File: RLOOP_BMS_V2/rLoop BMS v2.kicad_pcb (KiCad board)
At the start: 2 copper layers, 77.5 x 133 mm, 274 parts, among them IC1 FXO-HC736R-1.000, IC2 SN74AUP1G74DCUR, IC3 ATA6870N-PLQW-1, IC4 ATA6870N-PLQW-1, IC5 ATA6870N-PLQW-1, J1 CONN_02X07, J2 2-640387-0, Q1 FDN337N, Q10 PMV20ENR, Q11 PMV20ENR, Q12 PMV20ENR, Q13 PMV20ENR, Q14 PMV20ENR, Q15 PMV20ENR, Q16 PMV20ENR, Q17 PMV20ENR, Q18 PMV20ENR, Q19 PMV20ENR, Q2 PMV20ENR, Q3 PMV20ENR, Q4 PMV20ENR, Q5 PMV20ENR, Q6 PMV20ENR, Q7 PMV20ENR, Q8 PMV20ENR, Q9 PMV20ENR, U1 VOS618A-2X001T

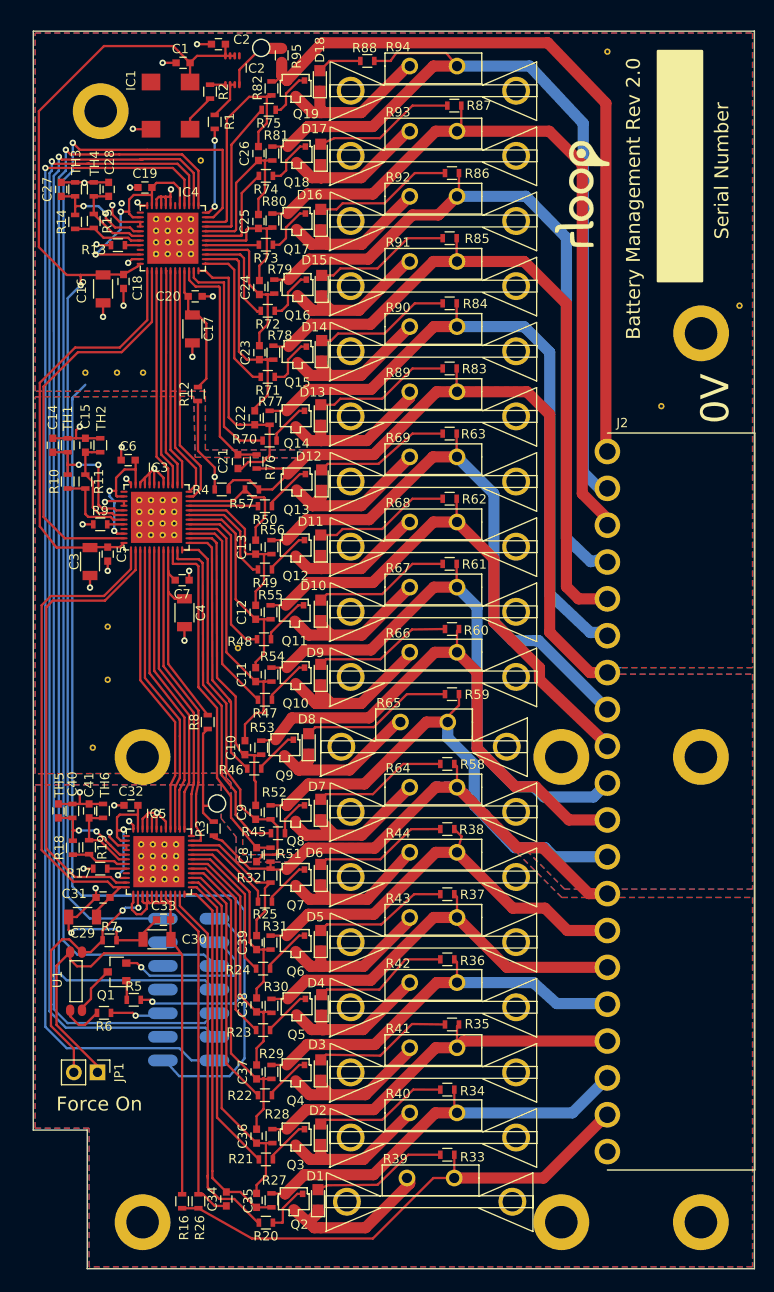
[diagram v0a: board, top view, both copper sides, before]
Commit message: Ti BMS WIP
Getting there. Need to add temp sensors, fan control, and an LDO for the
SPI ISO supply.
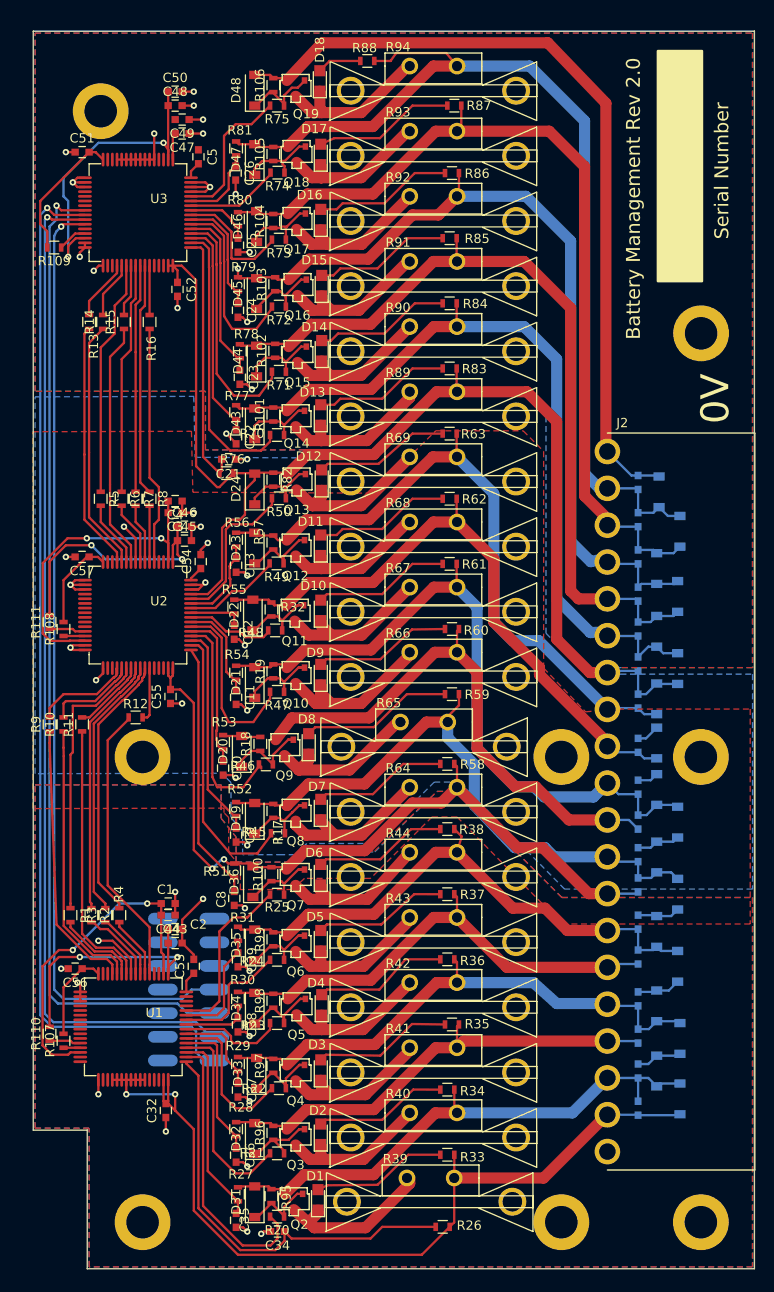
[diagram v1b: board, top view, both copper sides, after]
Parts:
- removed G***: LOGO, rLoop_Footprints:rLoop_Logo
- removed IC1: FXO-HC736R-1.000, rLoop_Footprints:Oscillator_SMD_FOX_HC3_4pin_7.0x5.0mm
- removed IC2: SN74AUP1G74DCUR, rLoop_Footprints:TI_sn74aup1g74_UQFN-0.6mm
- removed IC3, IC4, IC5: ATA6870N-PLQW-1, rLoop_Footprints:ATA6870-QFN48
- removed JP1: Debug Jumper, Pin_Headers:Pin_Header_Straight_1x02_Pitch2.54mm
- removed Q1: FDN337N, TO_SOT_Packages_SMD:SOT-23
- removed the REF** at (67.0, 64.5)
- removed the REF** at (65.7, 64.5)
- removed the REF** at (64.5, 64.5)
- removed the REF** at (63.2, 64.5)
- removed the REF** at (67.0, 63.2)
- removed the REF** at (65.7, 63.2)
- removed the REF** at (64.5, 63.2)
- removed the REF** at (63.2, 63.2)
- removed the REF** at (65.2, 97.2)
- removed the REF** at (63.9, 97.2)
- removed the REF** at (67.0, 67.0)
- removed the REF** at (62.6, 97.2)
- removed the REF** at (61.4, 97.2)
- removed the REF** at (65.2, 95.9)
- removed the REF** at (63.9, 95.9)
- removed the REF** at (62.6, 95.9)
- removed the REF** at (61.4, 95.9)
- removed the REF** at (65.2, 94.7)
- removed the REF** at (63.9, 94.7)
- removed the REF** at (62.6, 94.7)
- removed the REF** at (61.4, 94.7)
- removed the REF** at (65.7, 67.0)
- removed the REF** at (65.2, 93.4)
- removed the REF** at (63.9, 93.4)
- removed the REF** at (62.6, 93.4)
- removed the REF** at (61.4, 93.4)
- removed the REF** at (65.3, 134.2)
- removed the REF** at (64.1, 134.2)
- removed the REF** at (62.9, 134.2)
- removed the REF** at (61.6, 134.2)
- removed the REF** at (65.3, 132.9)
- removed the REF** at (64.1, 132.9)
- removed the REF** at (64.5, 67.0)
- removed the REF** at (62.9, 132.9)
- removed the REF** at (61.6, 132.9)
- removed the REF** at (65.3, 131.7)
- removed the REF** at (64.1, 131.7)
- removed the REF** at (62.9, 131.7)
- removed the REF** at (61.6, 131.7)
- removed the REF** at (65.3, 130.4)
- removed the REF** at (64.1, 130.4)
- removed the REF** at (62.9, 130.4)
- removed the REF** at (61.6, 130.4)
- removed the REF** at (63.2, 67.0)
- removed the REF** at (117.5, 83.3)
- removed the REF** at (125.9, 72.5)
- removed the REF** at (111.7, 45.2)
- removed the REF** at (72.0, 109.3)
- removed the REF** at (56.4, 120.0)
- removed the REF** at (58.0, 112.7)
- removed the REF** at (58.0, 107.0)
- removed the REF** at (61.8, 79.7)
- removed the REF** at (59.0, 79.7)
- removed the REF** at (55.6, 79.7)
- removed the REF** at (67.0, 65.7)
- removed the REF** at (68.0, 56.9)
- removed the REF** at (65.7, 65.7)
- removed the REF** at (64.5, 65.7)
- removed the REF** at (63.2, 65.7)
- removed TH1, TH2, TH3, TH4, TH5, TH6: NTCS0603E3103JLT, Resistors_SMD:R_0603
- added C42: .1 uF / 50v / SMD 0603, Capacitors_SMD:C_0603, B.Cu at (115.0, 91.5)
- added C43: 2.2 uF / 50V/ 10% / SMD 0603, Capacitors_SMD:C_0603, F.Cu at (65.2, 141.0)
- added C44: .1 uF / 50V/ 10% / SMD 0603, Capacitors_SMD:C_0603, F.Cu at (64.5, 138.0)
- added C45: 2.2 uF / 50V/ 10% / SMD 0603, Capacitors_SMD:C_0603, F.Cu at (66.2, 97.8)
- added C46: .1 uF / 50V/ 10% / SMD 0603, Capacitors_SMD:C_0603, F.Cu at (66.2, 96.2)
- added C47: 2.2uF / 50V/ 10% / SMD 0603, Capacitors_SMD:C_0603, F.Cu at (66.0, 54.0)
- added C48: 2.2uF / 50V/ 10% / SMD 0603, Capacitors_SMD:C_0603, F.Cu at (65.2, 51.0)
- added C49: .1 uF / 50V/ 10% / SMD 0603, Capacitors_SMD:C_0603, F.Cu at (66.0, 52.5)
- added C50: .1 uF / 50V/ 10% / SMD 0603, Capacitors_SMD:C_0603, F.Cu at (65.2, 49.5)
- added C51: 2.2uF / 50V/ 10% / SMD 0603, Capacitors_SMD:C_0603, F.Cu at (55.2, 56.0)
- added C52: .1uF / 50V/ 10% / SMD 0603, Capacitors_SMD:C_0603, F.Cu at (65.5, 70.8)
- added C53: 10 uF / 10V/ 10% / SMD 0603, Capacitors_SMD:C_0603, F.Cu at (67.2, 143.5)
- added C54: 10 uF / 10V/ 10% / SMD 0603, Capacitors_SMD:C_0603, F.Cu at (68.0, 100.0)
- added C55: 100n / 50V / 10% / SMD 0603, Capacitors_SMD:C_0603, F.Cu at (64.8, 114.5)
- added C56: 2.2uF / 50V/ 10% / SMD 0603, Capacitors_SMD:C_0603, F.Cu at (54.5, 143.8)
- added C57: 2.2uF / 50V/ 10% / SMD 0603, Capacitors_SMD:C_0603, F.Cu at (55.2, 99.5)
- added D19: 5.1 V / SOD-123, Diodes_SMD:D_SOD-123, F.Cu at (73.8, 127.6)
- added D20: 5.1 V / SOD-123, Diodes_SMD:D_SOD-123, F.Cu at (72.4, 120.4)
- added D21: 5.1 V / SOD-123, Diodes_SMD:D_SOD-123, F.Cu at (73.8, 113.0)
- added D22: 5.1 V / SOD-123, Diodes_SMD:D_SOD-123, F.Cu at (73.6, 105.8)
- added D23: 5.1 V / SOD-123, Diodes_SMD:D_SOD-123, F.Cu at (73.8, 98.5)
- added D24: 5.1 V / SOD-123, Diodes_SMD:D_SOD-123, F.Cu at (73.8, 92.2)
- added D25: 5.1 V / SOD-123, Diodes_SMD:D_SOD-123, B.Cu at (119.2, 135.8)
- added D26: 5.1 V / SOD-123, Diodes_SMD:D_SOD-123, B.Cu at (117.0, 131.8)
- added D27: 5.1 V / SOD-123, Diodes_SMD:D_SOD-123, B.Cu at (119.2, 128.0)
- added D28: 5.1 V / SOD-123, Diodes_SMD:D_SOD-123, B.Cu at (117.0, 124.5)
- added D29: 5.1 V / SOD-123, Diodes_SMD:D_SOD-123, B.Cu at (117.0, 119.5)
- added D30: 5.1 V / SOD-123, Diodes_SMD:D_SOD-123, B.Cu at (117.0, 114.8)
- added D31: 5.1 VDC / SOD-123, Diodes_SMD:D_SOD-123, F.Cu at (73.8, 168.8)
- added D32: 5.1 VDC / SOD-123, Diodes_SMD:D_SOD-123, F.Cu at (73.8, 162.0)
- added D33: 5.1 VDC / SOD-123, Diodes_SMD:D_SOD-123, F.Cu at (74.0, 155.0)
- added D34: 5.1 VDC / SOD-123, Diodes_SMD:D_SOD-123, F.Cu at (73.8, 148.0)
- added D35: 5.1 VDC / SOD-123, Diodes_SMD:D_SOD-123, F.Cu at (73.8, 141.2)
- added D36: 5.1 VDC / SOD-123, Diodes_SMD:D_SOD-123, F.Cu at (73.6, 134.4)
- added D37: 5.1 VDC / SOD-123, Diodes_SMD:D_SOD-123, B.Cu at (119.5, 157.8)
- added D38: 5.1 VDC / SOD-123, Diodes_SMD:D_SOD-123, B.Cu at (117.0, 154.8)
- added D39: 5.1 VDC / SOD-123, Diodes_SMD:D_SOD-123, B.Cu at (119.5, 151.2)
- added D40: 5.1 VDC / SOD-123, Diodes_SMD:D_SOD-123, B.Cu at (117.0, 147.8)
- added D41: 5.1 VDC / SOD-123, Diodes_SMD:D_SOD-123, B.Cu at (119.2, 143.5)
- added D42: 5.1 VDC / SOD-123, Diodes_SMD:D_SOD-123, B.Cu at (117.0, 139.8)
- added D43: 5.1 V / SOD-123, Diodes_SMD:D_SOD-123, F.Cu at (73.8, 85.2)
- added D44: 5.1 V / SOD-123, Diodes_SMD:D_SOD-123, F.Cu at (74.0, 78.5)
- added D45: 5.1 V / SOD-123, Diodes_SMD:D_SOD-123, F.Cu at (74.0, 71.2)
- added D46: 5.1 V / SOD-123, Diodes_SMD:D_SOD-123, F.Cu at (74.0, 64.0)
- added D47: 5.1 V / SOD-123, Diodes_SMD:D_SOD-123, F.Cu at (73.8, 56.8)
- added D48: 5.1 V / SOD-123, Diodes_SMD:D_SOD-123, F.Cu at (73.8, 49.4)
- added D49: 5.1 V / SOD-123, Diodes_SMD:D_SOD-123, B.Cu at (119.2, 111.5)
- added D50: 5.1 V / SOD-123, Diodes_SMD:D_SOD-123, B.Cu at (117.0, 107.5)
- added D51: 5.1 V / SOD-123, Diodes_SMD:D_SOD-123, B.Cu at (119.2, 103.8)
- added D52: 5.1 V / SOD-123, Diodes_SMD:D_SOD-123, B.Cu at (117.0, 100.8)
- added D53: 5.1 V / SOD-123, Diodes_SMD:D_SOD-123, B.Cu at (119.5, 96.8)
- added D54: 5.1 V / SOD-123, Diodes_SMD:D_SOD-123, B.Cu at (117.2, 92.5)
- added R100: 1M / 0.063W / 1% / SMD 0603, Resistors_SMD:R_0603, F.Cu at (75.6, 133.6)
- added R101: 1M / 0.063W / 1% / SMD 0603, Resistors_SMD:R_0603, F.Cu at (75.8, 84.2)
- added R102: 1M / 0.063W / 1% / SMD 0603, Resistors_SMD:R_0603, F.Cu at (76.0, 77.3)
- added R103: 1M / 0.063W / 1% / SMD 0603, Resistors_SMD:R_0603, F.Cu at (76.0, 70.2)
- added R104: 1M / 0.063W / 1% / SMD 0603, Resistors_SMD:R_0603, F.Cu at (75.8, 63.4)
- added R105: 1M / 0.063W / 1% / SMD 0603, Resistors_SMD:R_0603, F.Cu at (75.8, 56.2)
- added R106: 1M / 0.063W / 1% / SMD 0603, Resistors_SMD:R_0603, F.Cu at (75.8, 48.8)
- added R107: 100K0 / 0.063W / 5% / SMD 0603, Resistors_SMD:R_0603, F.Cu at (53.2, 151.5)
- added R108: 100K0 / 0.063W / 5% / SMD 0603, Resistors_SMD:R_0603, F.Cu at (53.2, 107.2)
- added R109: 100K0 / 0.063W / 5% / SMD 0603, Resistors_SMD:R_0603, F.Cu at (52.2, 66.2)
- added R110: 100K0 / 0.063W / 5% / SMD 0603, Resistors_SMD:R_0603, F.Cu at (51.8, 150.8)
- added R111: 100K0 / 0.063W / 5% / SMD 0603, Resistors_SMD:R_0603, F.Cu at (51.8, 106.5)
- added R96: 1M / 0.063W / 1% / SMD 0603, Resistors_SMD:R_0603, F.Cu at (75.8, 161.4)
- added R97: 1M / 0.063W / 1% / SMD 0603, Resistors_SMD:R_0603, F.Cu at (75.8, 154.2)
- added R98: 1M / 0.063W / 1% / SMD 0603, Resistors_SMD:R_0603, F.Cu at (75.8, 147.2)
- added R99: 1M / 0.063W / 1% / SMD 0603, Resistors_SMD:R_0603, F.Cu at (75.8, 140.6)
- added U2: bq76PL536A_HTQFP, rLoop_Footprints:bq76pl536a, F.Cu at (61.2, 105.8)
- added U3: bq76PL536A_HTQFP, rLoop_Footprints:bq76pl536a, F.Cu at (61.2, 62.5)
- C1: value 100n / 50V / 10% / SMD 0603 -> 2.2 uF / 50V/ 10% / SMD 0603
- C14, C15, C40, C41: value 100n -> .1 uF / 50v / SMD 0603; moved to B.Cu
- C16, C17, C30: value 10uF / 25V / 20% / SMD 1206 -> .1 uF / 50v / SMD 0603; footprint Capacitors_SMD:C_1206 -> Capacitors_SMD:C_0603; moved to B.Cu
- C18, C20: value 100nF / 50V / 10% / SMD 0603 -> .1 uF / 50V / SMD 0603; moved to B.Cu
- C19: value 100n / 50V / 10% / SMD 0603 -> .1 uF / 50V / SMD 0603; moved to B.Cu
- C2: value 100n / 50V / 10% / SMD 0603 -> .1 uF / 50V/ 10% / SMD 0603
- C27, C28: value 100n -> .1 uF / 50V / SMD 0603; moved to B.Cu
- C29: value 10uF / 25V / 20% / SMD 1206 -> .1 uF / 50V / SMD 0603; footprint Capacitors_SMD:C_1206 -> Capacitors_SMD:C_0603; moved to B.Cu
- C3: value 10uF / 25V / 20% / SMD 1206 -> 2.2 uF / 50V/ 10% / SMD 0603; footprint Capacitors_SMD:C_1206 -> Capacitors_SMD:C_0603
- C31, C33, C7: value 100nF / 50V / 10% / SMD 0603 -> .1 uF / 50v / SMD 0603; moved to B.Cu
- C4: value 10uF / 25V / 20% / SMD 1206 -> .1 uF / 50V/ 10% / SMD 0603; footprint Capacitors_SMD:C_1206 -> Capacitors_SMD:C_0603
- C5: value 100nF / 50V / 10% / SMD 0603 -> 10 uF / 10V/ 10% / SMD 0603
- C6: value 100n / 50V / 10% / SMD 0603 -> .1 uF / 50v / SMD 0603; moved to B.Cu
- J1: value CONN_02X07 -> 1241050-7
- R1: value 47R / .1 W / 1% / SMD 0603 -> 1K0 / 0.063W / 1% / SMD 0603
- R10, R11, R14, R15: value 10K / .1 W / 1% / SMD 0603 -> 1K0 / 0.063W / 1% / SMD 0603
- R12, R16, R8: value 10 -> 1K0 / 0.063W / 1% / SMD 0603
- R13, R9: value 121K / 0.1W / 1% / SMD 0603 -> 1K0 / 0.063W / 1% / SMD 0603
- R17: value 121K / 0.1W / 1% / SMD 0603 -> 1M / .063W / 1% / SMD 0603
- R18, R19: value 10K / .1 W / 1% / SMD 0603 -> 1M / .063W / 1% / SMD 0603
- R2: value 47R / .1W / 1% / SMD 0603 -> 1K0 / 0.063W / 1% / SMD 0603
- R3, R4: value 10R / 0.125W / 1% / SMD 0603 -> 1K0 / 0.063W / 1% / SMD 0603
- R32, R57, R82: value 1K0 / 0.063W / 1% / SMD 0603 -> 1M / .063W / 1% / SMD 0603
- R5: value 1k -> 1K0 / 0.063W / 1% / SMD 0603
- R6: value 270R / 0.1W / 5% / SMD 0603 -> 1K0 / 0.063W / 1% / SMD 0603
- R7: value 2.2K / 0.1W / 1% / SMD 0603 -> 1K0 / 0.063W / 1% / SMD 0603
- R95: value 10R / 0.125W / 1% / SMD 0603 -> 1M / 0.063W / 1% / SMD 0603
- U1: value VOS618A-2X001T -> bq76PL536A_HTQFP; footprint rLoop_Footprints:VOS618A-2X001T -> rLoop_Footprints:bq76pl536a
- moved R95 122.6 mm to (75.6, 168.2)
- moved C19 108.7 mm to (115.0, 154.8), turned to 90 degrees
- moved C27 106.8 mm to (115.0, 147.0)
- moved C18 104.7 mm to (115.0, 158.8), turned to 90 degrees
- moved C28 100.2 mm to (115.0, 142.5)
- moved C2 95.2 mm to (65.2, 139.5)
- moved R16 94.6 mm to (62.5, 74.2)
- moved C20 92.7 mm to (115.0, 151.0), turned to 90 degrees
- moved C1 90.4 mm to (64.5, 136.8)
- moved R2 89.4 mm to (56.2, 138.0)
- moved R1 86.6 mm to (54.0, 138.0)
- moved C16 75.6 mm to (115.0, 119.8), turned to 90 degrees
- moved C14 74.8 mm to (115.0, 128.0)
- moved C6 71.3 mm to (115.0, 134.8), turned to 90 degrees
- moved C15 69.8 mm to (115.0, 124.2)
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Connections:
- C1 pad 1: /Clock Generator/VDD -> GND_3
- C1 pad 2: GND_1 -> Net-(C1-Pad2)
- C10 pad 2: /CONTROLLER 2/MBAT4 -> GND_2
- C11 pad 2: /CONTROLLER 2/MBAT3 -> GND_2
- C12 pad 2: /CONTROLLER 2/MBAT2 -> GND_2
- C13 pad 2: /CONTROLLER 2/MBAT1 -> GND_2
- C14 pad 1: Net-(C14-Pad1) -> /DISCHARGE_2/CELL_4
- C14 pad 2: GND_2 -> /DISCHARGE_2/CELL_3
- C15 pad 1: Net-(C15-Pad1) -> /DISCHARGE_2/CELL_3
- C15 pad 2: GND_2 -> /DISCHARGE_2/CELL_2
- C16 pad 1: /Clock Generator/VDD -> /DISCHARGE_2/CELL_2
- C16 pad 2: GND_1 -> /DISCHARGE_2/CELL_1
- C17 pad 1: VDDHV_1 -> /DISCHARGE_2/CELL_1
- C17 pad 2: GND_1 -> VDDHV_1
- C18 pad 1: /Clock Generator/VDD -> VDDHV_3
- C18 pad 2: GND_1 -> /DISCHARGE_3/CELL_5
- C19 pad 1: GND_1 -> /DISCHARGE_3/CELL_5
- C19 pad 2: Net-(C19-Pad2) -> /DISCHARGE_3/CELL_4
- C2 pad 1: GND_1 -> LDOA_3
- C2 pad 2: /Clock Generator/VDD -> GND_3
- C20 pad 1: GND_1 -> /DISCHARGE_3/CELL_4
- C20 pad 2: VDDHV_1 -> /DISCHARGE_3/CELL_3
- C21 pad 2: /CONTROLLER 1/MBAT6 -> GND_1
- C22 pad 2: /CONTROLLER 1/MBAT5 -> GND_1
- C23 pad 2: /CONTROLLER 1/MBAT4 -> GND_1
- C24 pad 2: /CONTROLLER 1/MBAT3 -> GND_1
- C25 pad 2: /CONTROLLER 1/MBAT2 -> GND_1
- C26 pad 2: /CONTROLLER 1/MBAT1 -> GND_1
- C27 pad 1: Net-(C27-Pad1) -> /DISCHARGE_3/CELL_3
- C27 pad 2: GND_1 -> /DISCHARGE_3/CELL_2
- C28 pad 1: Net-(C28-Pad1) -> /DISCHARGE_3/CELL_2
- C28 pad 2: GND_1 -> /DISCHARGE_3/CELL_1
- C29 pad 1: /CONTROLLER 3/VDDHVM -> /DISCHARGE_3/CELL_1
- C3 pad 1: /CONTROLLER 2/VDDHVM -> GND_2
- C3 pad 2: GND_2 -> Net-(C3-Pad2)
- C30 pad 1: VDDHV_3 -> VDDHV_1
- C30 pad 2: GND_3 -> /DISCHARGE_1/CELL_5
- C31 pad 1: /CONTROLLER 3/VDDHVM -> /DISCHARGE_1/CELL_5
- C31 pad 2: GND_3 -> /DISCHARGE_1/CELL_4
- C32 pad 2: Net-(C32-Pad2) -> VDDHV_3
- C33 pad 1: GND_3 -> /DISCHARGE_1/CELL_4
- C33 pad 2: VDDHV_3 -> /DISCHARGE_1/CELL_3
- C34 pad 2: /CONTROLLER 3/MBAT6 -> GND_3
- C35 pad 2: /CONTROLLER 3/MBAT5 -> GND_3
- C36 pad 2: /CONTROLLER 3/MBAT4 -> GND_3
- C37 pad 2: /CONTROLLER 3/MBAT3 -> GND_3
- C38 pad 2: /CONTROLLER 3/MBAT2 -> GND_3
- C39 pad 2: /CONTROLLER 3/MBAT1 -> GND_3
- C4 pad 1: VDDHV_2 -> GND_2
- C4 pad 2: GND_2 -> Net-(C3-Pad2)
- C40 pad 1: Net-(C40-Pad1) -> /DISCHARGE_1/CELL_3
- C40 pad 2: GND_3 -> /DISCHARGE_1/CELL_2
- C41 pad 1: Net-(C41-Pad1) -> /DISCHARGE_1/CELL_2
- C41 pad 2: GND_3 -> /DISCHARGE_1/CELL_1
- C5 pad 1: /CONTROLLER 2/VDDHVM -> GND_1
- C5 pad 2: GND_2 -> Net-(C5-Pad2)
- C6 pad 1: GND_2 -> GND_3
- C6 pad 2: Net-(C6-Pad2) -> /DISCHARGE_2/CELL_5
- C7 pad 1: GND_2 -> /DISCHARGE_2/CELL_5
- C7 pad 2: VDDHV_2 -> /DISCHARGE_2/CELL_4
- C8 pad 2: /CONTROLLER 2/MBAT6 -> GND_2
- C9 pad 2: /CONTROLLER 2/MBAT5 -> GND_2
- J1 pad 14: /Clock Generator/VDD -> /MCU Connector/VDD_FROM_BMS
- J1 pad 7: /MCU Connector/NCS_FROM_PWR_NODE -> /CONTROLLER 1/CS_H
- J1 pad 9: /CONTROLLER 1/IRQ_OUT -> /MCU Connector/IRQ_TO_PWR_NODE
- J2 pad 10: /DISCHARGE Top/CELL_10 -> /DISCHARGE_2/CELL_4
- J2 pad 11: /DISCHARGE Top/CELL_9 -> /DISCHARGE_2/CELL_3
- J2 pad 12: /DISCHARGE Top/CELL_8 -> /DISCHARGE_2/CELL_2
- J2 pad 13: /DISCHARGE Top/CELL_7 -> /DISCHARGE_2/CELL_1
- J2 pad 14: /DISCHARGE Top/CELL_6 -> VDDHV_1
- J2 pad 15: /DISCHARGE Top/CELL_5 -> /DISCHARGE_1/CELL_5
- J2 pad 16: /DISCHARGE Top/CELL_4 -> /DISCHARGE_1/CELL_4
- J2 pad 17: /DISCHARGE Top/CELL_3 -> /DISCHARGE_1/CELL_3
- J2 pad 18: /DISCHARGE Top/CELL_2 -> /DISCHARGE_1/CELL_2
- J2 pad 19: /DISCHARGE Top/CELL_1 -> /DISCHARGE_1/CELL_1
- J2 pad 2: /DISCHARGE Top/CELL_18 -> VDDHV_3
- J2 pad 20: /DISCHARGE Top/CELL_0 -> GND_1
- J2 pad 3: /DISCHARGE Top/CELL_17 -> /DISCHARGE_3/CELL_5
- J2 pad 4: /DISCHARGE Top/CELL_16 -> /DISCHARGE_3/CELL_4
- J2 pad 5: /DISCHARGE Top/CELL_15 -> /DISCHARGE_3/CELL_3
- J2 pad 6: /DISCHARGE Top/CELL_14 -> /DISCHARGE_3/CELL_2
- J2 pad 7: /DISCHARGE Top/CELL_13 -> /DISCHARGE_3/CELL_1
- J2 pad 8: /DISCHARGE Top/CELL_12 -> GND_3
- J2 pad 9: /DISCHARGE Top/CELL_11 -> /DISCHARGE_2/CELL_5
- Q10 pad 1: Net-(Q10-Pad1) -> Net-(D21-Pad1)
- Q10 pad 2: /DISCHARGE Top/CELL_9 -> /DISCHARGE_2/CELL_3
- Q11 pad 1: Net-(Q11-Pad1) -> Net-(D22-Pad1)
- Q11 pad 2: /DISCHARGE Top/CELL_8 -> /DISCHARGE_2/CELL_2
- Q12 pad 1: Net-(Q12-Pad1) -> Net-(D23-Pad1)
- Q12 pad 2: /DISCHARGE Top/CELL_7 -> /DISCHARGE_2/CELL_1
- Q13 pad 1: Net-(Q13-Pad1) -> Net-(D24-Pad1)
- Q13 pad 2: /DISCHARGE Top/CELL_6 -> VDDHV_1
- Q14 pad 2: /DISCHARGE Top/CELL_5 -> /DISCHARGE_1/CELL_5
- Q15 pad 2: /DISCHARGE Top/CELL_4 -> /DISCHARGE_1/CELL_4
- Q16 pad 2: /DISCHARGE Top/CELL_3 -> /DISCHARGE_1/CELL_3
- Q17 pad 2: /DISCHARGE Top/CELL_2 -> /DISCHARGE_1/CELL_2
- Q18 pad 2: /DISCHARGE Top/CELL_1 -> /DISCHARGE_1/CELL_1
- Q19 pad 2: /DISCHARGE Top/CELL_0 -> GND_1
- Q2 pad 1: Net-(Q2-Pad1) -> Net-(D31-Pad1)
- Q2 pad 2: /DISCHARGE Top/CELL_17 -> /DISCHARGE_3/CELL_5
- Q3 pad 2: /DISCHARGE Top/CELL_16 -> /DISCHARGE_3/CELL_4
- Q4 pad 2: /DISCHARGE Top/CELL_15 -> /DISCHARGE_3/CELL_3
- Q5 pad 2: /DISCHARGE Top/CELL_14 -> /DISCHARGE_3/CELL_2
- Q6 pad 2: /DISCHARGE Top/CELL_13 -> /DISCHARGE_3/CELL_1
- Q7 pad 2: /DISCHARGE Top/CELL_12 -> GND_3
- Q8 pad 1: Net-(Q8-Pad1) -> Net-(D19-Pad1)
- Q8 pad 2: /DISCHARGE Top/CELL_11 -> /DISCHARGE_2/CELL_5
- Q9 pad 1: Net-(Q9-Pad1) -> Net-(D20-Pad1)
- Q9 pad 2: /DISCHARGE Top/CELL_10 -> /DISCHARGE_2/CELL_4
- R1 pad 1: /Clock Generator/CLK_500K -> Net-(R1-Pad1)
- R1 pad 2: Net-(IC2-Pad2) -> /CONTROLLER 2/SDO_N
- R10 pad 1: Net-(IC3-Pad31) -> /CONTROLLER 2/SDI_N
- R10 pad 2: Net-(C14-Pad1) -> Net-(R10-Pad2)
- R11 pad 1: Net-(C15-Pad1) -> /CONTROLLER 2/SCLK_N
- R11 pad 2: Net-(IC3-Pad31) -> Net-(R11-Pad2)
- R12 pad 1: GND_2 -> /CONTROLLER 2/CONV_N
- R12 pad 2: VDDHV_1 -> Net-(R12-Pad2)
- R13 pad 1: GND_1 -> /CONTROLLER 1/CS_N
- R14 pad 1: Net-(IC4-Pad31) -> /CONTROLLER 1/SDI_N
- R14 pad 2: Net-(C27-Pad1) -> Net-(R14-Pad2)
- R15 pad 1: Net-(C28-Pad1) -> /CONTROLLER 1/SCLK_N
- R15 pad 2: Net-(IC4-Pad31) -> Net-(R15-Pad2)
- R16 pad 1: /DISCHARGE Top/CELL_18 -> /CONTROLLER 1/CONV_N
- R16 pad 2: VDDHV_3 -> Net-(R16-Pad2)
- R17 pad 1: GND_3 -> Net-(D19-Pad1)
- R17 pad 2: Net-(IC5-Pad32) -> /DISCHARGE_2/CELL_5
- R18 pad 1: Net-(IC5-Pad31) -> Net-(D20-Pad1)
- R18 pad 2: Net-(C40-Pad1) -> /DISCHARGE_2/CELL_4
- R19 pad 1: Net-(C41-Pad1) -> Net-(D21-Pad1)
- R19 pad 2: Net-(IC5-Pad31) -> /DISCHARGE_2/CELL_3
- R2 pad 1: Net-(IC2-Pad1) -> /CONTROLLER 2/FAULT_N
- R2 pad 2: Net-(IC1-Pad3) -> Net-(R2-Pad2)
- R20 pad 1: Net-(Q2-Pad1) -> Net-(D31-Pad1)
- R20 pad 2: /DISCHARGE Top/DISCHARGE_3_6 -> /DISCHARGE_3/DISCHARGE_6
- R21 pad 2: /DISCHARGE Top/DISCHARGE_3_5 -> /DISCHARGE_3/DISCHARGE_5
- R22 pad 2: /DISCHARGE Top/DISCHARGE_3_4 -> /DISCHARGE_3/DISCHARGE_4
- R23 pad 2: /DISCHARGE Top/DISCHARGE_3_3 -> /DISCHARGE_3/DISCHARGE_3
- R24 pad 2: /DISCHARGE Top/DISCHARGE_3_2 -> /DISCHARGE_3/DISCHARGE_2
- R25 pad 2: /DISCHARGE Top/DISCHARGE_3_1 -> /DISCHARGE_3/DISCHARGE_1
- R26 pad 1: /DISCHARGE Top/CELL_18 -> VDDHV_3
- R27 pad 1: /DISCHARGE Top/CELL_17 -> /DISCHARGE_3/CELL_5
- R28 pad 1: /DISCHARGE Top/CELL_16 -> /DISCHARGE_3/CELL_4
- R29 pad 1: /DISCHARGE Top/CELL_15 -> /DISCHARGE_3/CELL_3
- R3 pad 1: /DISCHARGE Top/CELL_12 -> Net-(R3-Pad1)
- R3 pad 2: GND_3 -> /CONTROLLER 2/ALERT_N
- R30 pad 1: /DISCHARGE Top/CELL_14 -> /DISCHARGE_3/CELL_2
- R31 pad 1: /DISCHARGE Top/CELL_13 -> /DISCHARGE_3/CELL_1
- R32 pad 1: /DISCHARGE Top/CELL_12 -> Net-(D22-Pad1)
- R32 pad 2: /CONTROLLER 3/MBAT1 -> /DISCHARGE_2/CELL_2
- R33 pad 1: /DISCHARGE Top/CELL_18 -> VDDHV_3
- R34 pad 1: /DISCHARGE Top/CELL_17 -> /DISCHARGE_3/CELL_5
- R35 pad 1: /DISCHARGE Top/CELL_16 -> /DISCHARGE_3/CELL_4
- R36 pad 1: /DISCHARGE Top/CELL_15 -> /DISCHARGE_3/CELL_3
- R37 pad 1: /DISCHARGE Top/CELL_14 -> /DISCHARGE_3/CELL_2
- R38 pad 1: /DISCHARGE Top/CELL_13 -> /DISCHARGE_3/CELL_1
- R39 pad 1: /DISCHARGE Top/CELL_18 -> VDDHV_3
- R4 pad 1: /DISCHARGE Top/CELL_6 -> Net-(R4-Pad1)
- R4 pad 2: GND_2 -> /CONTROLLER 2/DRDY_N
- R40 pad 1: /DISCHARGE Top/CELL_17 -> /DISCHARGE_3/CELL_5
- R41 pad 1: /DISCHARGE Top/CELL_16 -> /DISCHARGE_3/CELL_4
- R42 pad 1: /DISCHARGE Top/CELL_15 -> /DISCHARGE_3/CELL_3
- R43 pad 1: /DISCHARGE Top/CELL_14 -> /DISCHARGE_3/CELL_2
- R44 pad 1: /DISCHARGE Top/CELL_13 -> /DISCHARGE_3/CELL_1
- R45 pad 1: Net-(Q8-Pad1) -> Net-(D19-Pad1)
- R45 pad 2: /DISCHARGE Top/DISCHARGE_2_6 -> /DISCHARGE_2/DISCHARGE_6
- R46 pad 1: Net-(Q9-Pad1) -> Net-(D20-Pad1)
- R46 pad 2: /DISCHARGE Top/DISCHARGE_2_5 -> /DISCHARGE_2/DISCHARGE_5
- R47 pad 1: Net-(Q10-Pad1) -> Net-(D21-Pad1)
- R47 pad 2: /DISCHARGE Top/DISCHARGE_2_4 -> /DISCHARGE_2/DISCHARGE_4
- R48 pad 1: Net-(Q11-Pad1) -> Net-(D22-Pad1)
- R48 pad 2: /DISCHARGE Top/DISCHARGE_2_3 -> /DISCHARGE_2/DISCHARGE_3
- R49 pad 1: Net-(Q12-Pad1) -> Net-(D23-Pad1)
- R49 pad 2: /DISCHARGE Top/DISCHARGE_2_2 -> /DISCHARGE_2/DISCHARGE_2
- R5 pad 1: Net-(Q1-Pad1) -> /CONTROLLER 1/SDO_N
- R5 pad 2: /MCU Connector/POWER_DN_DISABLE_FROM_PWR_NODE -> Net-(R5-Pad2)
- R50 pad 1: Net-(Q13-Pad1) -> Net-(D24-Pad1)
- R50 pad 2: /DISCHARGE Top/DISCHARGE_2_1 -> /DISCHARGE_2/DISCHARGE_1
- R51 pad 1: /DISCHARGE Top/CELL_12 -> GND_3
- R52 pad 1: /DISCHARGE Top/CELL_11 -> /DISCHARGE_2/CELL_5
- R53 pad 1: /DISCHARGE Top/CELL_10 -> /DISCHARGE_2/CELL_4
- R54 pad 1: /DISCHARGE Top/CELL_9 -> /DISCHARGE_2/CELL_3
- R55 pad 1: /DISCHARGE Top/CELL_8 -> /DISCHARGE_2/CELL_2
- R56 pad 1: /DISCHARGE Top/CELL_7 -> /DISCHARGE_2/CELL_1
- R57 pad 1: /DISCHARGE Top/CELL_6 -> Net-(D23-Pad1)
- R57 pad 2: /CONTROLLER 2/MBAT1 -> /DISCHARGE_2/CELL_1
- R58 pad 1: /DISCHARGE Top/CELL_12 -> GND_3
- R59 pad 1: /DISCHARGE Top/CELL_11 -> /DISCHARGE_2/CELL_5
- R6 pad 1: MCU_3V3 -> /CONTROLLER 1/FAULT_N
- R60 pad 1: /DISCHARGE Top/CELL_10 -> /DISCHARGE_2/CELL_4
- R61 pad 1: /DISCHARGE Top/CELL_9 -> /DISCHARGE_2/CELL_3
- R62 pad 1: /DISCHARGE Top/CELL_8 -> /DISCHARGE_2/CELL_2
- R63 pad 1: /DISCHARGE Top/CELL_7 -> /DISCHARGE_2/CELL_1
- R64 pad 1: /DISCHARGE Top/CELL_12 -> GND_3
- R65 pad 1: /DISCHARGE Top/CELL_11 -> /DISCHARGE_2/CELL_5
- R66 pad 1: /DISCHARGE Top/CELL_10 -> /DISCHARGE_2/CELL_4
- R67 pad 1: /DISCHARGE Top/CELL_9 -> /DISCHARGE_2/CELL_3
- R68 pad 1: /DISCHARGE Top/CELL_8 -> /DISCHARGE_2/CELL_2
- R69 pad 1: /DISCHARGE Top/CELL_7 -> /DISCHARGE_2/CELL_1
- R7 pad 1: /PWR_DN_DISABLE/PWR_DN_BMS -> /CONTROLLER 1/ALERT_N
- R7 pad 2: GND_3 -> Net-(R7-Pad2)
- R70 pad 2: /DISCHARGE Top/DISCHARGE_1_6 -> /DISCHARGE_1/DISCHARGE_6
- R71 pad 2: /DISCHARGE Top/DISCHARGE_1_5 -> /DISCHARGE_1/DISCHARGE_5
- R72 pad 2: /DISCHARGE Top/DISCHARGE_1_4 -> /DISCHARGE_1/DISCHARGE_4
- R73 pad 2: /DISCHARGE Top/DISCHARGE_1_3 -> /DISCHARGE_1/DISCHARGE_3
- R74 pad 2: /DISCHARGE Top/DISCHARGE_1_2 -> /DISCHARGE_1/DISCHARGE_2
- R75 pad 2: /DISCHARGE Top/DISCHARGE_1_1 -> /DISCHARGE_1/DISCHARGE_1
- R76 pad 1: /DISCHARGE Top/CELL_6 -> VDDHV_1
- R77 pad 1: /DISCHARGE Top/CELL_5 -> /DISCHARGE_1/CELL_5
- R78 pad 1: /DISCHARGE Top/CELL_4 -> /DISCHARGE_1/CELL_4
- R79 pad 1: /DISCHARGE Top/CELL_3 -> /DISCHARGE_1/CELL_3
- R8 pad 1: GND_3 -> /CONTROLLER 1/DRDY_N
- R8 pad 2: VDDHV_2 -> Net-(R8-Pad2)
- R80 pad 1: /DISCHARGE Top/CELL_2 -> /DISCHARGE_1/CELL_2
- R81 pad 1: /DISCHARGE Top/CELL_1 -> /DISCHARGE_1/CELL_1
- R82 pad 1: /DISCHARGE Top/CELL_0 -> Net-(D24-Pad1)
- R82 pad 2: /CONTROLLER 1/MBAT1 -> VDDHV_1
- R83 pad 1: /DISCHARGE Top/CELL_6 -> VDDHV_1
- R84 pad 1: /DISCHARGE Top/CELL_5 -> /DISCHARGE_1/CELL_5
- R85 pad 1: /DISCHARGE Top/CELL_4 -> /DISCHARGE_1/CELL_4
- R86 pad 1: /DISCHARGE Top/CELL_3 -> /DISCHARGE_1/CELL_3
- R87 pad 1: /DISCHARGE Top/CELL_2 -> /DISCHARGE_1/CELL_2
- R88 pad 1: /DISCHARGE Top/CELL_1 -> /DISCHARGE_1/CELL_1
- R89 pad 1: /DISCHARGE Top/CELL_6 -> VDDHV_1
- R9 pad 1: GND_2 -> /CONTROLLER 2/CS_N
- R90 pad 1: /DISCHARGE Top/CELL_5 -> /DISCHARGE_1/CELL_5
- R91 pad 1: /DISCHARGE Top/CELL_4 -> /DISCHARGE_1/CELL_4
- R92 pad 1: /DISCHARGE Top/CELL_3 -> /DISCHARGE_1/CELL_3
- R93 pad 1: /DISCHARGE Top/CELL_2 -> /DISCHARGE_1/CELL_2
- R94 pad 1: /DISCHARGE Top/CELL_1 -> /DISCHARGE_1/CELL_1
- R95 pad 1: /DISCHARGE Top/CELL_0 -> Net-(D31-Pad1)
- R95 pad 2: GND_1 -> /DISCHARGE_3/CELL_5
- U1 pad 1: Net-(R6-Pad2) -> /CONTROLLER 3/MBAT7
- U1 pad 2: Net-(Q1-Pad3) -> /DISCHARGE_3/DISCHARGE_6
- U1 pad 3: /PWR_DN_DISABLE/PWR_DN_BMS -> /CONTROLLER 3/MBAT6
- U1 pad 4: VDDHV_3 -> /DISCHARGE_3/DISCHARGE_5
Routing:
- net /Clock Generator/VDD: track 134.5 -> 0.00 mm, vias 1 -> 0
- net /CONTROLLER 1/IRQ_OUT: track 128.2 -> 0.00 mm, vias 1 -> 0
- net /MCU Connector/NCS_FROM_PWR_NODE: track 125.2 -> 0.00 mm, vias 1 -> 0
- net VDDHV_1: track 14.2 -> 132.3 mm
- net /DISCHARGE_1/CELL_1: track 0.00 -> 106.2 mm
- net /CONTROLLER 1/CS_H: track 0.00 -> 103.0 mm, vias 0 -> 1
- net /DISCHARGE_1/CELL_2: track 0.00 -> 96.0 mm
- net /DISCHARGE_1/CELL_3: track 0.00 -> 92.5 mm, vias 0 -> 1
- net /DISCHARGE Top/CELL_1: track 91.0 -> 0.00 mm
- net /DISCHARGE_1/CELL_4: track 0.00 -> 89.3 mm
- net /DISCHARGE_1/CELL_5: track 0.00 -> 85.6 mm
- net /DISCHARGE Top/CELL_2: track 81.3 -> 0.00 mm
- net /DISCHARGE Top/CELL_0: track 79.9 -> 0.00 mm
- net /DISCHARGE Top/CELL_6: track 78.5 -> 0.00 mm
- net /DISCHARGE Top/CELL_3: track 77.1 -> 0.00 mm
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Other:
- board text removed: "Force On"

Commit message: More WIP on BMS v2.5
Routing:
- net /CONTROLLER 1/CS_N: track 26.7 -> 29.9 mm
- net /CONTROLLER 2/CS_N: track 29.6 -> 31.9 mm
- net /CONTROLLER 1/SDI_N: track 27.1 -> 28.9 mm
- net /CONTROLLER 2/SDI_N: track 29.5 -> 31.1 mm
- net /CONTROLLER 2/SDO_N: track 29.8 -> 30.8 mm
- net /CONTROLLER 1/SDO_N: track 25.4 -> 26.3 mm

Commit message: More BMS v2.5 WIP
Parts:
- added C58: .047 uF / 50V/ 10% / SMD 0603, Capacitors_SMD:C_0603, F.Cu at (60.8, 131.2)
- added C59: .047 uF / 50V/ 10% / SMD 0603, Capacitors_SMD:C_0603, F.Cu at (63.0, 162.2)
- added C60: .047 uF / 50V/ 10% / SMD 0603, Capacitors_SMD:C_0603, F.Cu at (63.1, 87.8)
- added C61: .047 uF / 50V/ 10% / SMD 0603, Capacitors_SMD:C_0603, F.Cu at (66.3, 117.0)
- added C62: .047 uF / 50V/ 10% / SMD 0603, Capacitors_SMD:C_0603, F.Cu at (61.4, 48.8)
- added C63: .047 uF / 50V/ 10% / SMD 0603, Capacitors_SMD:C_0603, F.Cu at (65.5, 78.5)
- added C64: 1uF / 100V / SMD0603, Capacitors_SMD:C_0603, F.Cu at (116.2, 172.5)
- added C65: .1uF / 100V / SMD0603, Capacitors_SMD:C_0603, F.Cu at (113.0, 170.0)
- added R112: 1.47k / 0.063W / 1% / SMD 0603, Resistors_SMD:R_0603, F.Cu at (61.5, 133.4)
- added R113: 1.82k / 0.063W / 1% / SMD 0603, Resistors_SMD:R_0603, F.Cu at (61.5, 135.0)
- added R114: 1.47k / 0.063W / 1% / SMD 0603, Resistors_SMD:R_0603, F.Cu at (62.2, 160.0)
- added R115: 1.82k / 0.063W / 1% / SMD 0603, Resistors_SMD:R_0603, F.Cu at (62.2, 158.2)
- added R116: 1.82k / 0.063W / 1% / SMD0603, Resistors_SMD:R_0603, F.Cu at (63.8, 90.0)
- added R117: 1.82k / 0.063W / 1% / SMD0603, Resistors_SMD:R_0603, F.Cu at (63.8, 91.5)
- added R118: 1.82k / 0.063W / 1% / SMD0603, Resistors_SMD:R_0603, F.Cu at (65.0, 117.0)
- added R119: 1.82k / 0.063W / 1% / SMD0603, Resistors_SMD:R_0603, F.Cu at (63.4, 115.0)
- added R120: 1.47k / 0.063W / 1% / SMD0603, Resistors_SMD:R_0603, F.Cu at (62.1, 51.0)
- added R121: 1.82k / 0.063W / 1% / SMD0603, Resistors_SMD:R_0603, F.Cu at (62.1, 52.6)
- added R122: 1.47k / 0.063W / 1% / SMD0603, Resistors_SMD:R_0603, F.Cu at (64.8, 76.0)
- added R123: 1.82k / 0.063W / 1% / SMD0603, Resistors_SMD:R_0603, F.Cu at (64.8, 74.2)
- added TH1: 10k / 1% / 3454K / SMD0603, Resistors_SMD:R_0603, F.Cu at (62.4, 131.2)
- added TH2: 10k / 1% / 3454K / SMD0603, Resistors_SMD:R_0603, F.Cu at (61.5, 162.2)
- added TH3: 10k / 1% / 3454K / SMD0603, Resistors_SMD:R_0603, F.Cu at (64.5, 87.8)
- added TH4: 10k / 1% / 3454K / SMD0603, Resistors_SMD:R_0603, F.Cu at (66.3, 119.8)
- added TH5: 10k / 1% / 3454K / SMD0603, Resistors_SMD:R_0603, F.Cu at (63.0, 48.8)
- added TH6: 10k / 1% / 3454K / SMD0603, Resistors_SMD:R_0603, F.Cu at (64.0, 78.2)
- added U4: MIC5282-5.0YMM, rLoop_Footprints:MIC5282, F.Cu at (113.0, 172.5)
- moved R12 2.26 mm to (58.8, 117.0)
- moved R5 2.06 mm to (55.2, 92.8)
- moved R6 2.06 mm to (57.5, 92.8)
- moved R7 2.06 mm to (59.0, 92.8)
- moved R8 2.06 mm to (60.5, 92.8)
- moved C55 1.49 mm to (65.8, 113.4), turned to 180 degrees
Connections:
- J1 pad 14: /MCU Connector/VDD_FROM_BMS -> /ISO POWER/5V_ISO
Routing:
- net GND_1: track 123.3 -> 217.7 mm
- net 5V_2: track 10.0 -> 59.6 mm, vias 0 -> 4
- net 5V_3: track 9.81 -> 48.7 mm, vias 0 -> 4
- net 5V_1: track 14.6 -> 52.7 mm, vias 0 -> 2
- net /CONTROLLER 1/CS_H: track 103.0 -> 125.8 mm
- net /MCU Connector/SCK_FROM_PWR_NODE: track 106.9 -> 127.7 mm
- net VDDHV_3: track 96.4 -> 114.0 mm, vias 2 -> 3
- net /MCU Connector/MOSI_FROM_PWR_NODE: track 109.1 -> 126.2 mm
- net GND_3: track 118.3 -> 132.7 mm
- net Net-(C58-Pad1): track 0.00 -> 13.3 mm
- net /MCU Connector/MISO_TO_PWR_NODE: track 113.5 -> 126.3 mm
- net Net-(C60-Pad1): track 0.00 -> 12.0 mm
- net Net-(C63-Pad1): track 0.00 -> 10.4 mm
- net Net-(R113-Pad1): track 0.00 -> 10.4 mm
- net Net-(R117-Pad1): track 0.00 -> 9.58 mm
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
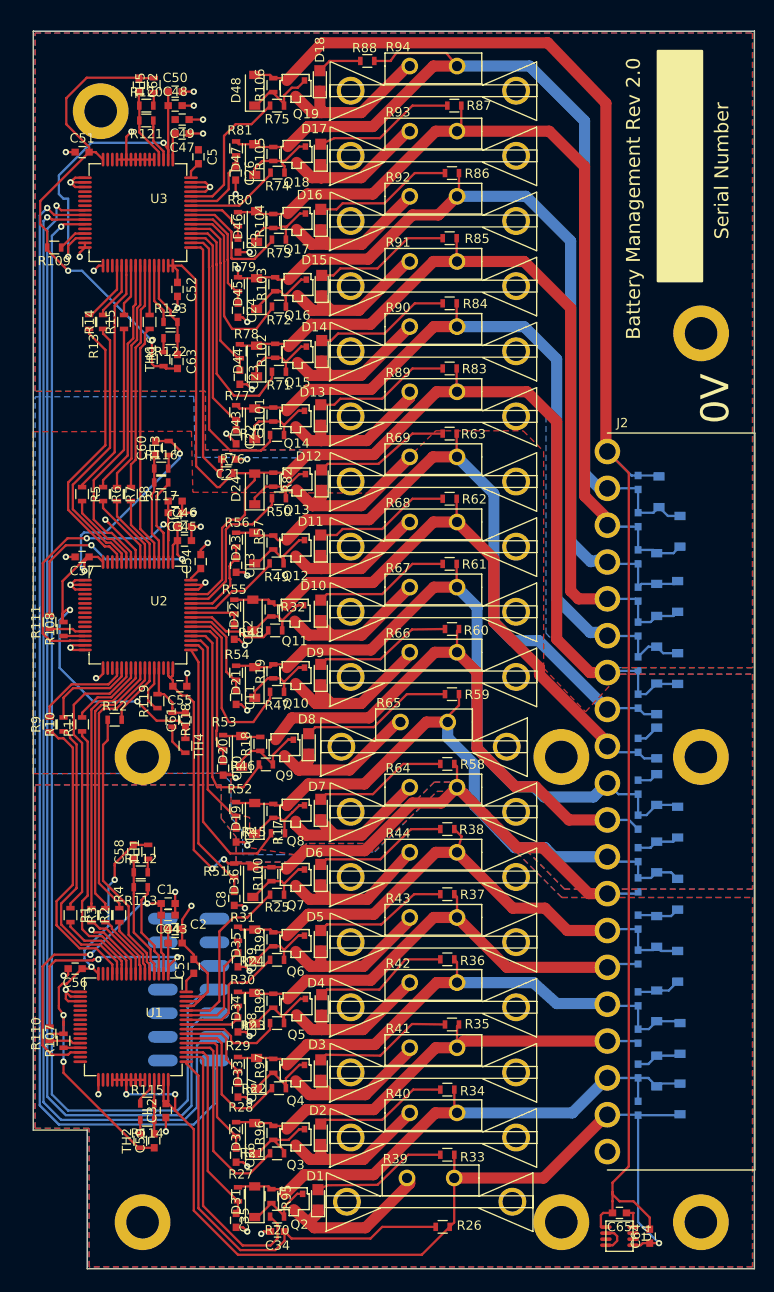
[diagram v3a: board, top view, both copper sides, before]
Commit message: more WIP
making room for a thermal pad and power circuits
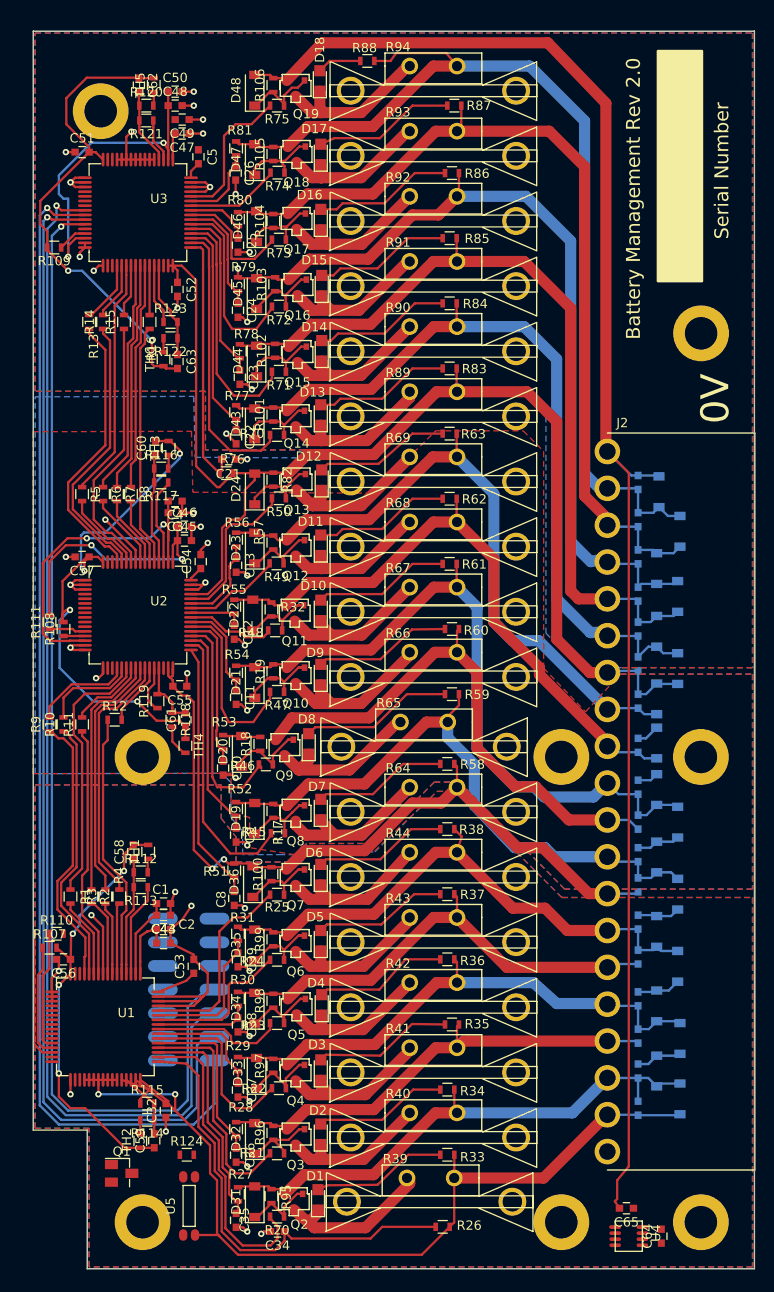
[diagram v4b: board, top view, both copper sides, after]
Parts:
- added Q1: VOS618A-2X001T, TO_SOT_Packages_SMD:SuperSOT-3, F.Cu at (59.5, 165.8)
- added R124: 270R / 0.1W / 5% / SMD 0603, Resistors_SMD:R_0603, F.Cu at (66.5, 163.8)
- added U5: VOS618A-2X001T, rLoop_Footprints:VOS618A-2X001T, F.Cu at (66.8, 169.2)
- moved R110 10.8 mm to (52.5, 140.0), turned to 0 degrees
- moved R107 10.1 mm to (51.8, 141.5), turned to 0 degrees
- moved U1 3.00 mm to (57.8, 150.0)
- moved R1 2.00 mm to (54.0, 136.0)
- moved R2 2.00 mm to (56.2, 136.0)
- moved R3 2.00 mm to (57.8, 136.0)
- moved R4 2.00 mm to (59.2, 136.0)
- moved C56 1.60 mm to (53.2, 142.8)
- moved C2 1.25 mm to (64.0, 139.5)
- moved C43 1.25 mm to (64.0, 141.0)
- moved C64 1.25 mm to (117.5, 172.5)
- moved U4 1.00 mm to (114.0, 172.5)
- moved C65 0.90 mm to (113.8, 169.5)
- moved C1 0.50 mm to (64.0, 136.8)
- moved C44 0.50 mm to (64.0, 138.0)
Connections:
- C64 pad 1: VDDHV_3 -> Net-(C64-Pad1)
- J1 pad 13: /MCU Connector/POWER_DN_DISABLE_FROM_PWR_NODE -> /ISO POWER/COMMS_EN
- U4 pad 1: VDDHV_3 -> Net-(C64-Pad1)
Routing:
- net LDOA_3: track 27.7 -> 7.48 mm, vias 2 -> 0
- net Net-(C1-Pad2): track 36.3 -> 23.2 mm, vias 2 -> 0
- net Net-(R107-Pad1): track 1.80 -> 12.2 mm
- net GND_1: track 217.7 -> 208.0 mm
- net Net-(R110-Pad1): track 3.40 -> 12.9 mm
- net VDDHV_3: track 114.0 -> 105.0 mm, vias 3 -> 2
- net GND_3: track 132.7 -> 140.9 mm, vias 15 -> 14
- net /ISO POWER/5V_ISO: track 3.25 -> 0.00 mm
- net /CONTROLLER 3/MBAT6: track 20.7 -> 23.9 mm
- net /DISCHARGE_3/DISCHARGE_2: track 13.4 -> 16.4 mm
- net /CONTROLLER 3/MBAT3: track 7.14 -> 10.1 mm
- net /DISCHARGE_3/DISCHARGE_5: track 21.8 -> 24.8 mm
- net /DISCHARGE_3/DISCHARGE_4: track 16.4 -> 19.4 mm
- net /DISCHARGE_3/DISCHARGE_3: track 11.2 -> 14.2 mm
- net /DISCHARGE_3/DISCHARGE_1: track 18.6 -> 21.6 mm
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
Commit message: BMS v2.5 more WIP
so close, all traces routed.
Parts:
- moved C64 5.89 mm to (111.7, 171.8)
- moved Q1 4.86 mm to (64.0, 163.8), turned to 270 degrees
- moved R115 4.01 mm to (58.2, 158.5)
- moved C59 4.00 mm to (59.0, 162.2)
- moved R114 4.00 mm to (58.2, 160.0)
- moved TH2 4.00 mm to (57.5, 162.2)
- moved C65 3.70 mm to (116.0, 172.4), turned to 90 degrees
- moved C32 2.69 mm to (63.2, 156.5), turned to 180 degrees
- moved U5 1.24 mm to (67.7, 170.1)
- moved R124 1.01 mm to (67.0, 164.6)
- moved R110 0.75 mm to (52.5, 139.2)
- turned U4 to 0 degrees
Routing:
- net /ISO POWER/5V_ISO: track 0.00 -> 101.2 mm, vias 0 -> 1
- net GND_1: track 208.0 -> 297.2 mm, vias 17 -> 18
- net Net-(C64-Pad1): track 0.00 -> 49.2 mm
- net /ISO POWER/COMMS_EN: track 0.00 -> 29.4 mm, vias 0 -> 1
- net MCU_GND: track 0.00 -> 28.9 mm, vias 0 -> 1
- net MCU_3V3: track 0.00 -> 23.3 mm, vias 0 -> 1
- net Net-(C1-Pad2): track 23.2 -> 42.1 mm, vias 0 -> 2
- net LDOA_3: track 7.48 -> 22.4 mm, vias 0 -> 2
- net VDDHV_3: track 105.0 -> 99.3 mm
- net Net-(Q1-Pad3): track 0.00 -> 3.73 mm
- net Net-(R124-Pad2): track 0.00 -> 2.87 mm
- net /DISCHARGE_3/DISCHARGE_6: track 33.1 -> 30.9 mm
- net GND_3: track 140.9 -> 142.9 mm
- net /CONTROLLER 3/MBAT7: track 48.7 -> 46.8 mm
- net Net-(C47-Pad2): track 2.90 -> 4.40 mm
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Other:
- board size 77.5 x 133 mm -> 78 x 133 mm
